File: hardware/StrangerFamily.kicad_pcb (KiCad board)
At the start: 2 copper layers, 85 x 50 mm, 23 parts, among them J1 LCD_Conn, J2 Power_LEDs, J3 Output_LED, J5 Raspberry_Pi_zero, Q1 BSS138, Q2 BSS138, Q3 BSS138, Q4 BSS138

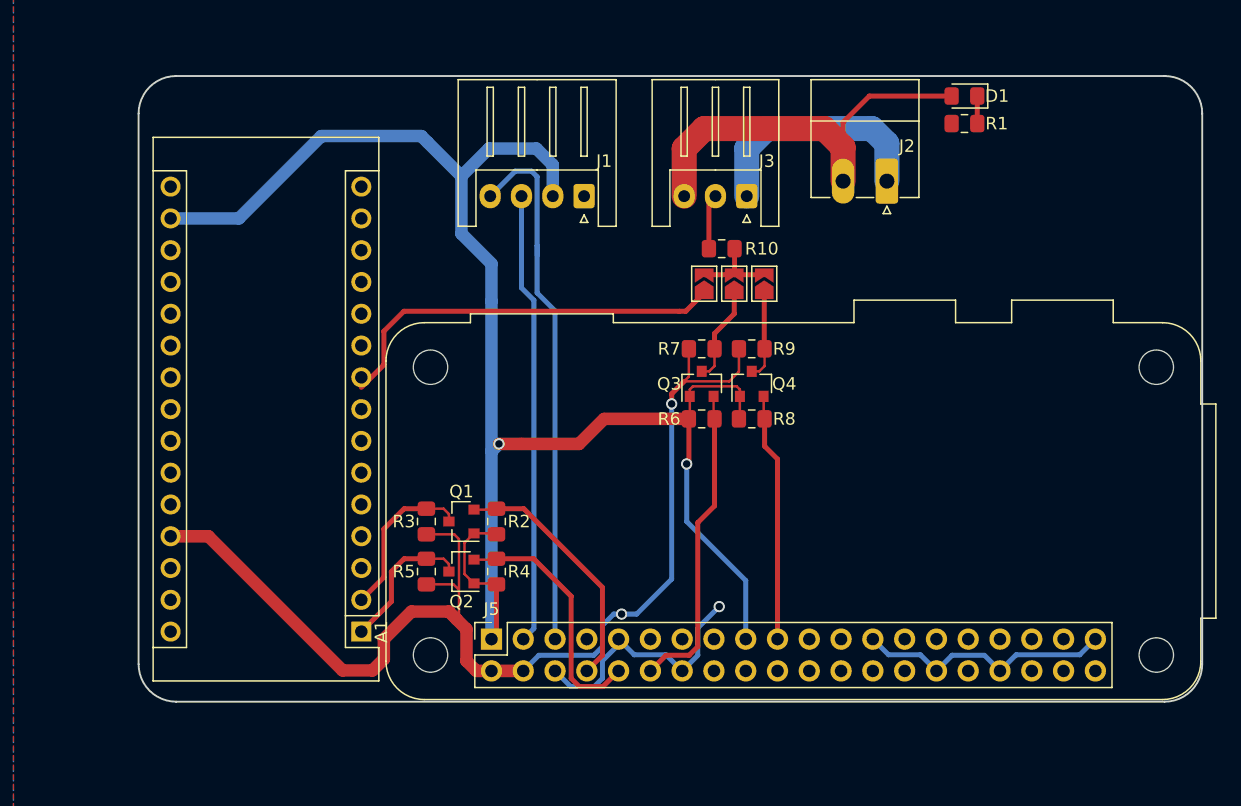
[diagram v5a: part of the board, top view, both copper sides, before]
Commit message: Fix raspberry pi missing sd card slot
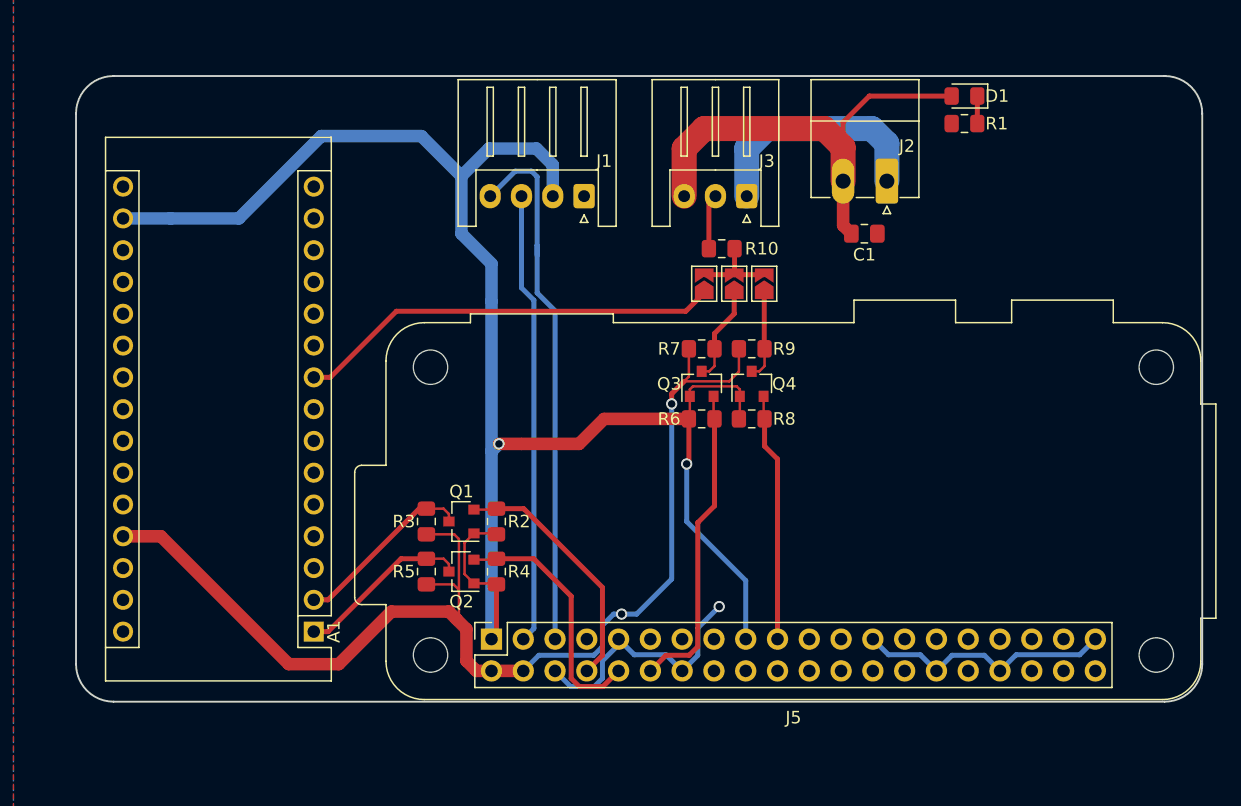
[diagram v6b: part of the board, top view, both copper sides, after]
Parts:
- added C1: C, Capacitor_SMD:C_0805_2012Metric_Pad1.18x1.45mm_HandSolder, F.Cu at (228.0, 82.6)
- J5: footprint Module:Raspberry_Pi_Zero_Socketed_THT_FaceDown_MountingHoles -> stranger_family_lib:Raspberry_Pi_Zero_Socketed_THT_FaceDown_MountingHoles
- moved A1 3.80 mm to (184.0, 114.4)
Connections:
- A1 pad 10: (no net) -> Net-(A1-Pad10)
- A1 pad 11: (no net) -> Net-(A1-Pad11)
- A1 pad 12: (no net) -> Net-(A1-Pad12)
- A1 pad 13: (no net) -> Net-(A1-Pad13)
- A1 pad 14: (no net) -> Net-(A1-Pad14)
- A1 pad 15: (no net) -> Net-(A1-Pad15)
- A1 pad 16: (no net) -> Net-(A1-Pad16)
- A1 pad 18: (no net) -> Net-(A1-Pad18)
- A1 pad 19: (no net) -> Net-(A1-Pad19)
- A1 pad 20: (no net) -> Net-(A1-Pad20)
- A1 pad 21: (no net) -> Net-(A1-Pad21)
- A1 pad 22: (no net) -> Net-(A1-Pad22)
- A1 pad 23: (no net) -> Net-(A1-Pad23)
- A1 pad 24: (no net) -> Net-(A1-Pad24)
- A1 pad 25: (no net) -> Net-(A1-Pad25)
- A1 pad 26: (no net) -> Net-(A1-Pad26)
- A1 pad 28: (no net) -> Net-(A1-Pad28)
- A1 pad 3: (no net) -> Net-(A1-Pad3)
- A1 pad 30: (no net) -> Net-(A1-Pad30)
- A1 pad 5: (no net) -> Net-(A1-Pad5)
- A1 pad 6: (no net) -> Net-(A1-Pad6)
- A1 pad 7: (no net) -> Net-(A1-Pad7)
- A1 pad 8: (no net) -> Net-(A1-Pad8)
- J5 pad 11: (no net) -> Net-(J5-Pad11)
- J5 pad 13: (no net) -> Net-(J5-Pad13)
- J5 pad 15: (no net) -> Net-(J5-Pad15)
- J5 pad 16: (no net) -> Net-(J5-Pad16)
- J5 pad 18: (no net) -> Net-(J5-Pad18)
- J5 pad 21: (no net) -> Net-(J5-Pad21)
- J5 pad 22: (no net) -> Net-(J5-Pad22)
- J5 pad 23: (no net) -> Net-(J5-Pad23)
- J5 pad 24: (no net) -> Net-(J5-Pad24)
- J5 pad 26: (no net) -> Net-(J5-Pad26)
- J5 pad 27: (no net) -> Net-(J5-Pad27)
- J5 pad 28: (no net) -> Net-(J5-Pad28)
- J5 pad 29: (no net) -> Net-(J5-Pad29)
- J5 pad 31: (no net) -> Net-(J5-Pad31)
- J5 pad 32: (no net) -> Net-(J5-Pad32)
- J5 pad 33: (no net) -> Net-(J5-Pad33)
- J5 pad 35: (no net) -> Net-(J5-Pad35)
- J5 pad 36: (no net) -> Net-(J5-Pad36)
- J5 pad 37: (no net) -> Net-(J5-Pad37)
- J5 pad 38: (no net) -> Net-(J5-Pad38)
- J5 pad 40: (no net) -> Net-(J5-Pad40)
- J5 pad 7: (no net) -> Net-(J5-Pad7)
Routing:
- net VDD: track 32.0 -> 36.5 mm
- net +3V3: track 134.9 -> 138.7 mm
- net +5V: track 92.5 -> 95.0 mm
- net /Nano_TX: track 11.6 -> 14.0 mm
- net /Arduino_out: track 32.1 -> 34.0 mm
- net /Nano_RX: track 13.1 -> 14.6 mm
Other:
- board size 85 x 50 mm -> 90 x 50 mm

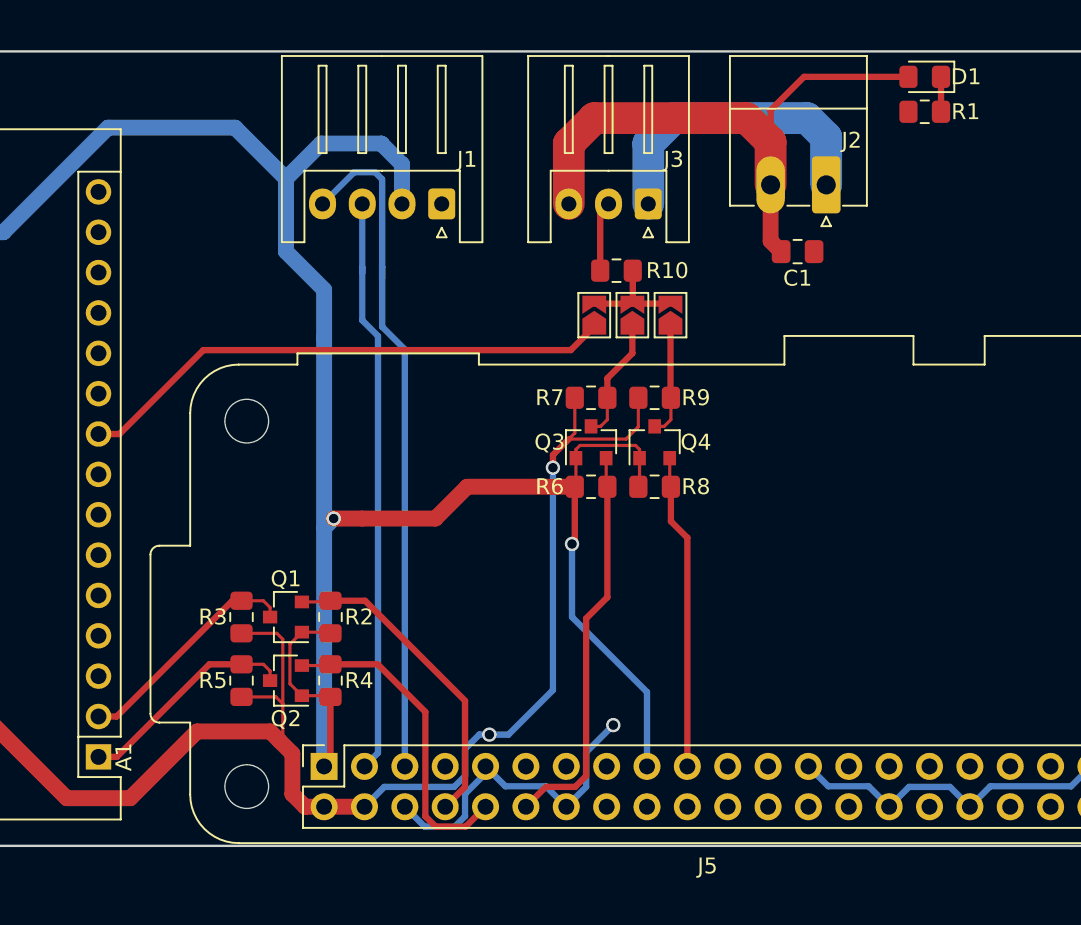
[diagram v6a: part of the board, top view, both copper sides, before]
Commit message: Fix electronics (schematics), use new components
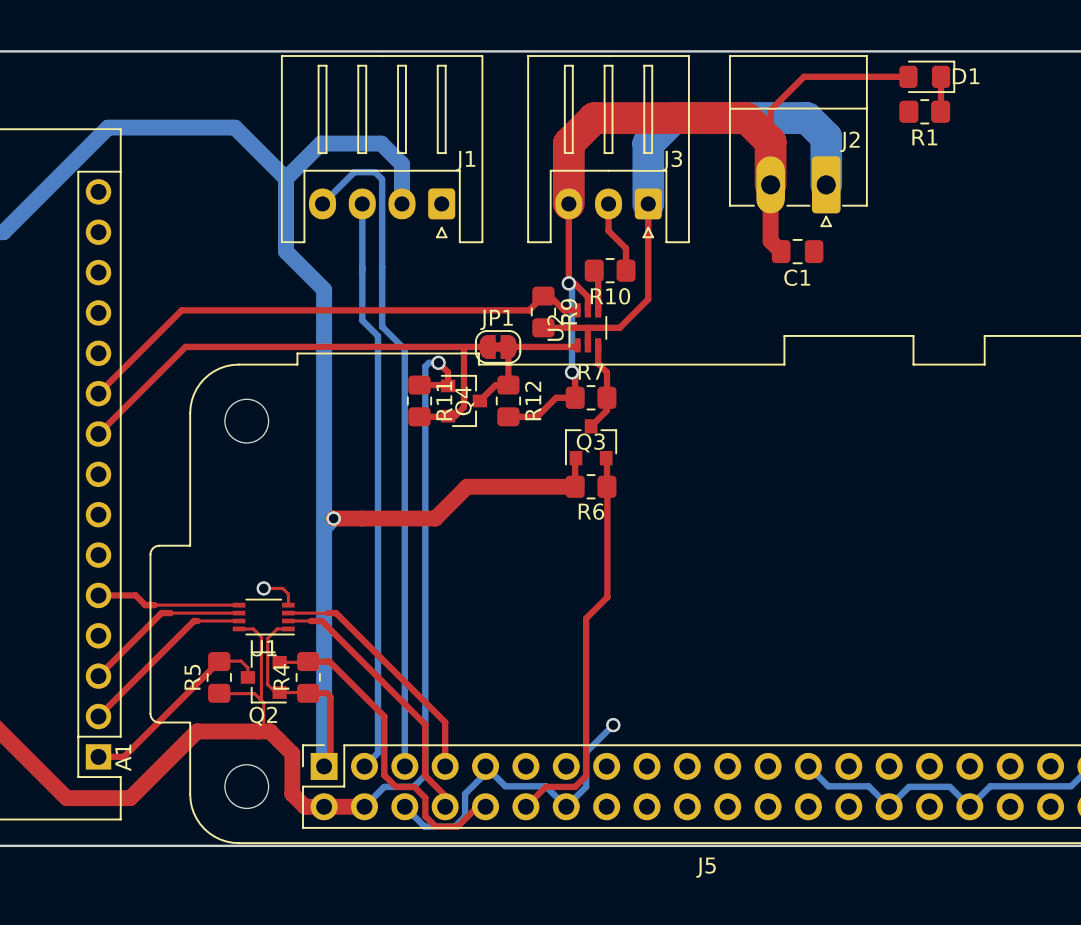
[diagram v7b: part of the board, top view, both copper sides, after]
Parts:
- removed JP2, JP3: Jumper_NC, Jumper:SolderJumper-2_P1.3mm_Open_TrianglePad1.0x1.5mm
- removed Q1: BSS138, Package_TO_SOT_SMD:SOT-23
- removed R2, R3, R8: 10k, Resistor_SMD:R_0805_2012Metric_Pad1.15x1.40mm_HandSolder
- added R11: 10k, Resistor_SMD:R_0805_2012Metric_Pad1.20x1.40mm_HandSolder, F.Cu at (204.2, 92.0)
- added R12: 10k, Resistor_SMD:R_0805_2012Metric_Pad1.20x1.40mm_HandSolder, F.Cu at (209.8, 92.0)
- added U1: 74LVC2T45DC, Package_SO:VSSOP-8_2.3x2mm_P0.5mm, F.Cu at (194.4, 105.6)
- added U2: 74LVC1G3157, Package_TO_SOT_SMD:Texas_R-PDSO-G6, F.Cu at (214.8, 87.4)
- JP1: value Jumper_NC -> Jumper; footprint Jumper:SolderJumper-2_P1.3mm_Open_TrianglePad1.0x1.5mm -> Jumper:SolderJumper-2_P1.3mm_Bridged_RoundedPad1.0x1.5mm
- R1, R10, R4, R5, R6, R7, R9: footprint Resistor_SMD:R_0805_2012Metric_Pad1.15x1.40mm_HandSolder -> Resistor_SMD:R_0805_2012Metric_Pad1.20x1.40mm_HandSolder
- moved Q4 12.3 mm to (207.0, 92.0), turned to 0 degrees
- moved R9 8.84 mm to (212.0, 86.4), turned to 270 degrees
- moved JP1 8.68 mm to (209.2, 88.6), turned to 180 degrees
- moved Q2 1.41 mm to (194.4, 109.4)
- moved R4 1.41 mm to (197.2, 109.4)
- moved R5 1.41 mm to (191.6, 109.4)
- moved R10 0.40 mm to (216.2, 83.8), turned to 180 degrees
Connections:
- A1 pad 10: Net-(A1-Pad10) -> /Arduino_is_out
- A1 pad 3: Net-(A1-Pad3) -> /Nano_~Reset
- A1 pad 5: Net-(A1-Pad5) -> /RX_enable
- C1 pad 2: VDD -> VCC
- D1 pad 2: VDD -> VCC
- J2 pad 2: VDD -> VCC
- J3 pad 3: VDD -> VCC
- J5 pad 17: +3V3 -> Net-(J5-Pad17)
- J5 pad 7: Net-(J5-Pad7) -> /RPi_Nano_~Reset
- JP1 pad 1: /PWM0_5V -> /Arduino_out_VDD
- JP1 pad 2: Net-(JP1-Pad2) -> /Arduino_out
- Q3 pad 3: /PWM0_5V -> /PWM0_VDD
- Q4 pad 1: +3V3 -> +5V
- Q4 pad 2: /MOSI -> /Arduino_out
- Q4 pad 3: /MOSI_5V -> /Arduino_out_VDD
- R10 pad 2: Net-(JP1-Pad2) -> Net-(R10-Pad2)
- R7 pad 1: +5V -> VCC
- R7 pad 2: /PWM0_5V -> /PWM0_VDD
- R9 pad 1: +5V -> /Arduino_is_out
- R9 pad 2: /MOSI_5V -> GND
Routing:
- net VCC: track 0.00 -> 56.0 mm, vias 0 -> 2
- net VDD: track 36.5 -> 0.00 mm
- net /Arduino_is_out: track 0.00 -> 33.1 mm
- net +3V3: track 138.7 -> 112.3 mm, vias 2 -> 1
- net /MOSI: track 19.9 -> 0.00 mm
- net GND: track 60.8 -> 77.7 mm, vias 1 -> 2
- net /RPi_Nano_~Reset: track 0.00 -> 15.5 mm
- net /Nano_~Reset: track 0.00 -> 10.5 mm
- net /RX_enable: track 0.00 -> 9.10 mm
- net /Arduino_out_VDD: track 0.00 -> 9.01 mm
- net +5V: track 95.0 -> 87.1 mm, vias 2 -> 1
- net /PWM0_5V: track 7.70 -> 0.00 mm
- net /MOSI_5V: track 7.06 -> 0.00 mm
- net Net-(JP1-Pad2): track 6.89 -> 0.00 mm
- net /PWM0_VDD: track 0.00 -> 5.74 mm
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
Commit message: v2 : use logos, move footprints
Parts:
- added G***: LOGO, stranger_family_lib:logo_klorydryk, F.Cu at (237.2, 110.6)
- added G***: LOGO, stranger_family_lib:logo_salamandar, F.Cu at (249.4, 111.2)
- added J4: LED_Out2, Connector_JST:JST_XH_S2B-XH-A_1x02_P2.50mm_Horizontal, F.Cu at (236.6, 79.6)
- added J6: LED_Out2, Connector_JST:JST_XH_S2B-XH-A_1x02_P2.50mm_Horizontal, F.Cu at (245.2, 79.6)
- moved J5 17.8 mm to (198.2, 97.2)
- moved R1 14.7 mm to (249.2, 80.2), turned to 270 degrees
- moved D1 14.2 mm to (250.2, 71.2)
- moved C1 13.8 mm to (214.2, 81.6)
- moved J2 13.2 mm to (216.6, 78.1)
- moved R10 9.51 mm to (225.4, 86.2), turned to 270 degrees
- moved J3 9.30 mm to (227.9, 79.6)
- moved U2 7.27 mm to (222.0, 88.4), turned to 0 degrees
- moved R9 6.94 mm to (218.8, 87.8)
- moved R7 5.32 mm to (220.3, 92.2), turned to 90 degrees
- moved R6 5.21 mm to (214.7, 92.2), turned to 270 degrees
- moved Q3 3.47 mm to (217.5, 92.2), turned to 0 degrees
- moved A1 3.40 mm to (184.0, 111.0)
- moved J1 1.32 mm to (206.9, 79.4)
- moved U1 0.60 mm to (194.4, 106.2)
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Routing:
- net +3V3: track 112.3 -> 68.0 mm, vias 1 -> 2
- net VCC: track 56.0 -> 93.4 mm, vias 2 -> 1
- net GND: track 77.7 -> 55.2 mm, vias 2 -> 3
- net /LCD_SLC: track 43.1 -> 24.7 mm
- net /LCD_SDA: track 36.5 -> 18.3 mm
- net +5V: track 87.1 -> 70.8 mm, vias 1 -> 2
- net /PWM0: track 25.2 -> 9.93 mm
- net Net-(D1-Pad1): track 2.20 -> 9.68 mm
- net /Arduino_is_out: track 33.1 -> 40.3 mm
- net /Arduino_out_VDD: track 9.01 -> 16.1 mm
- net /RPi_RX: track 21.4 -> 16.8 mm
- net /RPi_TX: track 17.0 -> 12.8 mm
- net /RX_enable: track 9.10 -> 10.9 mm
- net /Nano_RX: track 11.3 -> 9.68 mm
- net /Nano_TX: track 12.7 -> 11.0 mm
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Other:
- board text added: "3v3"
- board text added: "LCD"
- board text added: "LED Data"
- board text added: "LED Power"
- board text added: "SDA"
- board text added: "SLC"
- board text added: "StrangerBoard v2.1"
- board text added: "https://github.com/Salamandar/StrangerFamily"
